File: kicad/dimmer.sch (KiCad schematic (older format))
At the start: 13 parts, among them J3 Load Out, J4 LED_BYPASS, U2 MOC3021M, U3 4N25

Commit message: Add some more descriptive text
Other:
- note added: "Dimming"
- note added: "Zero Crossing Detection"
- moved on the sheet: D1, D3, J3, J4, R10, R8, U2
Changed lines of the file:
@@
 Wire Wire Line
 	7100 3800 7350 3800
-Text Label 6750 2650 3    60   ~ 0
+Text Label 6750 2550 3    60   ~ 0
 ZeroCrossingOut
 $Comp
 L MOC3021M U2
 U 1 1 59BAEACD
-P 5900 4650
-F 0 "U2" H 5690 4840 50  0000 L CNN
-F 1 "MOC3021M" H 5900 4850 50  0000 L CNN
-F 2 "Housings_DIP:DIP-6_W7.62mm_LongPads" H 5700 4450 50  0001 L CIN
-F 3 "" H 5875 4650 50  0001 L CNN
-	1    5900 4650
+P 5900 5150
+F 0 "U2" H 5690 5340 50  0000 L CNN
+F 1 "MOC3021M" H 5900 5350 50  0000 L CNN
+F 2 "Housings_DIP:DIP-6_W7.62mm_LongPads" H 5700 4950 50  0001 L CIN
+F 3 "" H 5875 5150 50  0001 L CNN
+	1    5900 5150
 	-1   0    0    -1
 $EndComp
@@
 L Q_TRIAC_AAG D1
 U 1 1 59BAECA2
-P 4200 4700
-F 0 "D1" H 4325 4725 50  0000 L CNN
-F 1 "BT136X-600" H 4325 4650 50  0000 L CNN
-F 2 "TO_SOT_Packages_THT:TO-220_Vertical" V 4275 4725 50  0001 C CNN
-F 3 "" V 4200 4700 50  0001 C CNN
-	1    4200 4700
-	1    0    0    -1
-$EndComp
-Wire Wire Line
-	3850 2600 3850 4550
-Wire Wire Line
-	3850 4550 4900 4550
+P 4200 5200
+F 0 "D1" H 4325 5225 50  0000 L CNN
+F 1 "BT136X-600" H 4325 5150 50  0000 L CNN
+F 2 "TO_SOT_Packages_THT:TO-220_Vertical" V 4275 5225 50  0001 C CNN
+F 3 "" V 4200 5200 50  0001 C CNN
+	1    4200 5200
+	1    0    0    -1
+$EndComp
+Wire Wire Line
+	3850 2600 3850 5050
+Wire Wire Line
+	3850 5050 4900 5050
 Connection ~ 3850 3600
 Wire Wire Line
-	4200 4850 4200 5150
-Text Label 4450 5150 0    60   ~ 0
+	4200 5350 4200 5650
+Text Label 4450 5650 0    60   ~ 0
 DimmedLiveOut
 Wire Wire Line
-	4200 5150 5400 5150
+	4200 5650 5400 5650
 $Comp
 L R R8
 U 1 1 59BAFEEA
-P 5050 4550
-F 0 "R8" V 5130 4550 50  0000 C CNN
-F 1 "1k" V 5050 4550 50  0000 C CNN
-F 2 "Resistors_THT:R_Axial_DIN0207_L6.3mm_D2.5mm_P7.62mm_Horizontal" V 4980 4550 50  0001 C CNN
-F 3 "" H 5050 4550 50  0001 C CNN
-	1    5050 4550
+P 5050 5050
+F 0 "R8" V 5130 5050 50  0000 C CNN
+F 1 "1k" V 5050 5050 50  0000 C CNN
+F 2 "Resistors_THT:R_Axial_DIN0207_L6.3mm_D2.5mm_P7.62mm_Horizontal" V 4980 5050 50  0001 C CNN
+F 3 "" H 5050 5050 50  0001 C CNN
+	1    5050 5050
 	0    1    1    0
 $EndComp
-Connection ~ 4200 4550
-Wire Wire Line
-	5200 4550 5600 4550
-Wire Wire Line
-	5600 4750 5600 4950
-Wire Wire Line
-	5600 4950 3950 4950
-Wire Wire Line
-	3950 4950 3950 4800
-Wire Wire Line
-	3950 4800 4050 4800
+Connection ~ 4200 5050
+Wire Wire Line
+	5200 5050 5600 5050
+Wire Wire Line
+	5600 5250 5600 5450
+Wire Wire Line
+	5600 5450 3950 5450
+Wire Wire Line
+	3950 5450 3950 5300
+Wire Wire Line
+	3950 5300 4050 5300
 $Comp
 L Conn_01x03 J3
 U 1 1 59BB0206
-P 5600 5250
-F 0 "J3" H 5600 5450 50  0000 C CNN
-F 1 "Load Out" H 5600 5050 50  0000 C CNN
-F 2 "kiall:RS_Pro_10mm_Pitch_3_Way_PCB_Terminal_Block" H 5600 5250 50  0001 C CNN
-F 3 "" H 5600 5250 50  0001 C CNN
-	1    5600 5250
-	1    0    0    -1
-$EndComp
-Wire Wire Line
-	3750 2400 3750 5350
-Wire Wire Line
-	3750 5350 5400 5350
+P 5600 5750
+F 0 "J3" H 5600 5950 50  0000 C CNN
+F 1 "Load Out" H 5600 5550 50  0000 C CNN
+F 2 "kiall:RS_Pro_10mm_Pitch_3_Way_PCB_Terminal_Block" H 5600 5750 50  0001 C CNN
+F 3 "" H 5600 5750 50  0001 C CNN
+	1    5600 5750
+	1    0    0    -1
+$EndComp
+Wire Wire Line
+	3750 2400 3750 5850
+Wire Wire Line
+	3750 5850 5400 5850
 Connection ~ 3750 4000
 $Comp
 L LED D3
 U 1 1 59BB07F2
-P 6600 4550
-F 0 "D3" H 6600 4650 50  0000 C CNN
-F 1 "LED" H 6600 4450 50  0000 C CNN
-F 2 "LEDs:LED_D4.0mm" H 6600 4550 50  0001 C CNN
-F 3 "" H 6600 4550 50  0001 C CNN
-	1    6600 4550
-	1    0    0    -1
-$EndComp
-Wire Wire Line
-	6200 4550 6450 4550
+P 6600 5050
+F 0 "D3" H 6600 5150 50  0000 C CNN
+F 1 "LED" H 6600 4950 50  0000 C CNN
+F 2 "LEDs:LED_D4.0mm" H 6600 5050 50  0001 C CNN
+F 3 "" H 6600 5050 50  0001 C CNN
+	1    6600 5050
+	1    0    0    -1
+$EndComp
+Wire Wire Line
+	6200 5050 6450 5050
 $Comp
 L R R10
 U 1 1 59BB08C6
-P 7050 4550
-F 0 "R10" V 7130 4550 50  0000 C CNN
-F 1 "220" V 7050 4550 50  0000 C CNN
-F 2 "Resistors_SMD:R_1206_HandSoldering" V 6980 4550 50  0001 C CNN
-F 3 "" H 7050 4550 50  0001 C CNN
-	1    7050 4550
+P 7050 5050
+F 0 "R10" V 7130 5050 50  0000 C CNN
+F 1 "220" V 7050 5050 50  0000 C CNN
+F 2 "Resistors_SMD:R_1206_HandSoldering" V 6980 5050 50  0001 C CNN
+F 3 "" H 7050 5050 50  0001 C CNN
+	1    7050 5050
 	0    1    1    0
 $EndComp
 Wire Wire Line
-	6750 4550 6900 4550
-Text Label 7700 3300 1    60   ~ 0
+	6750 5050 6900 5050
+Text Label 7700 2550 3    60   ~ 0
 DimmerIn
 $Sheet
@@
 L GND #PWR03
 U 1 1 59BB3317
-P 6350 4750
-F 0 "#PWR03" H 6350 4500 50  0001 C CNN
-F 1 "GND" H 6350 4600 50  0000 C CNN
-F 2 "" H 6350 4750 50  0001 C CNN
-F 3 "" H 6350 4750 50  0001 C CNN
-	1    6350 4750
-	1    0    0    -1
-$EndComp
-Wire Wire Line
-	6350 4750 6200 4750
+P 6350 5250
+F 0 "#PWR03" H 6350 5000 50  0001 C CNN
+F 1 "GND" H 6350 5100 50  0000 C CNN
+F 2 "" H 6350 5250 50  0001 C CNN
+F 3 "" H 6350 5250 50  0001 C CNN
+	1    6350 5250
+	1    0    0    -1
+$EndComp
+Wire Wire Line
+	6350 5250 6200 5250
 Wire Wire Line
 	6750 2500 6750 3800
@@
 	6200 2250 7700 2250
 Wire Wire Line
-	7700 2250 7700 4550
-Wire Wire Line
-	7700 4550 7200 4550
+	7700 2250 7700 5050
+Wire Wire Line
+	7700 5050 7200 5050
 Wire Wire Line
 	5000 2600 4550 2600
@@
 L GS2 J4
 U 1 1 59BD7F23
-P 6600 4350
-F 0 "J4" H 6700 4500 50  0000 C CNN
-F 1 "LED_BYPASS" V 6700 4201 50  0000 C CNN
-F 2 "Connectors:GS2" V 6674 4350 50  0001 C CNN
-F 3 "" H 6600 4350 50  0001 C CNN
-	1    6600 4350
+P 6600 4850
+F 0 "J4" H 6700 5000 50  0000 C CNN
+F 1 "LED_BYPASS" V 6700 4701 50  0000 C CNN
+F 2 "Connectors:GS2" V 6674 4850 50  0001 C CNN
+F 3 "" H 6600 4850 50  0001 C CNN
+	1    6600 4850
 	0    -1   -1   0
 $EndComp
 Wire Wire Line
-	6800 4350 6800 4550
-Connection ~ 6800 4550
-Wire Wire Line
-	6400 4350 6400 4550
-Connection ~ 6400 4550
+	6800 4850 6800 5050
+Connection ~ 6800 5050
+Wire Wire Line
+	6400 4850 6400 5050
+Connection ~ 6400 5050
 Wire Wire Line
 	5000 2200 3650 2200
 Wire Wire Line
-	3650 2200 3650 5250
-Wire Wire Line
-	3650 5250 5400 5250
+	3650 2200 3650 5750
+Wire Wire Line
+	3650 5750 5400 5750
+Wire Notes Line
+	3500 3350 7850 3350
+Wire Notes Line
+	3500 3350 3500 4350
+Wire Notes Line
+	3500 4350 7850 4350
+Wire Notes Line
+	7850 4350 7850 3350
+Wire Notes Line
+	7850 4650 3500 4650
+Wire Notes Line
+	3500 4650 3500 6100
+Wire Notes Line
+	3500 6100 7850 6100
+Wire Notes Line
+	7850 6100 7850 4650
+Text Notes 4000 3350 0    60   ~ 0
+Zero Crossing Detection
+Text Notes 4000 4650 0    60   ~ 0
+Dimming
 $EndSCHEMATC

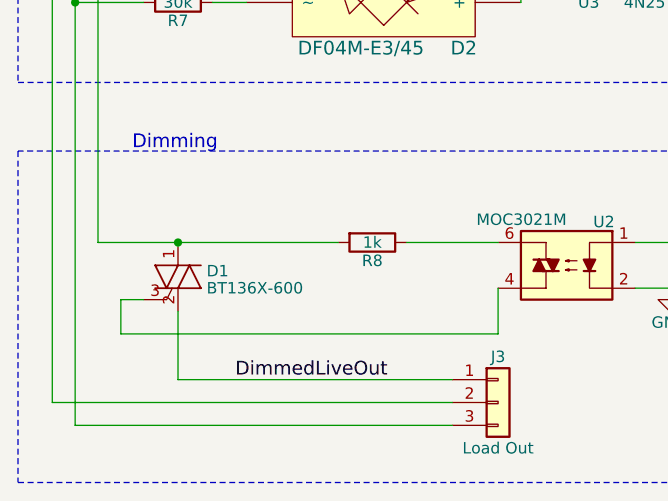
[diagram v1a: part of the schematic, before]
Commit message: Rev 1.1: Fix triac connections
Pins 1 and 2 on the triac D1 were connected in backwords, preventing
the circuit from working.
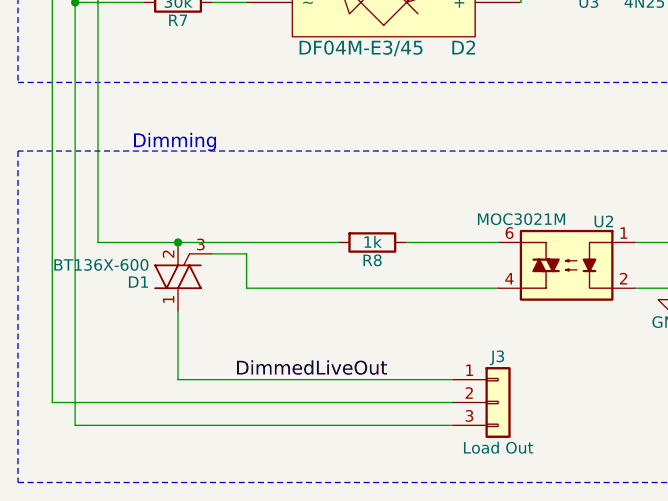
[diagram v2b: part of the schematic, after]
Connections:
- net DimmedLiveOut: now also D1.1 (A1); no longer D1.2 (A2)
- net at F1.2, R6.2, R8.2: now also D1.2 (A2); no longer D1.1 (A1)
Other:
- moved on the sheet: D1
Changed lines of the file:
@@
 Title "ESP8266 ESP-03 Lighting Dimmer"
 Date ""
-Rev "1.0"
+Rev "1.1"
 Comp "Kiall Mac Inness"
 Comment1 ""
@@
 F 3 "" V 4200 5200 50  0001 C CNN
 	1    4200 5200
-	1    0    0    -1
+	-1   0    0    1
 $EndComp
 Wire Wire Line
@@
 Wire Wire Line
 	5200 5050 5600 5050
-Wire Wire Line
-	5600 5250 5600 5450
-Wire Wire Line
-	5600 5450 3950 5450
-Wire Wire Line
-	3950 5450 3950 5300
-Wire Wire Line
-	3950 5300 4050 5300
 $Comp
 L Conn_01x03 J3
@@
 Text Notes 4000 4650 0    60   ~ 0
 Dimming
+Wire Wire Line
+	5600 5250 4500 5250
+Wire Wire Line
+	4500 5250 4500 5100
+Wire Wire Line
+	4500 5100 4350 5100
 $EndSCHEMATC

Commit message: Update for v1.2 - Fixes and board redesign
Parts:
- removed D3: LED, LEDs:LED_D4.0mm, symbol LED
- removed J4: LED_BYPASS, Connectors:GS2, symbol GS2
- D1: footprint TO_SOT_Packages_THT:TO-220_Vertical -> TO_SOT_Packages_THT:TO-220-3_Vertical
- U3: footprint Housings_DIP:DIP-6_W7.62mm_SMD -> Housings_DIP:SMDIP-6_W9.53mm
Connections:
- net at U2.1: now also R10.2
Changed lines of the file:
@@
 Title "ESP8266 ESP-03 Lighting Dimmer"
 Date ""
-Rev "1.1"
+Rev "1.2"
 Comp "Kiall Mac Inness"
 Comment1 ""
@@
 F 0 "U3" H 5950 4000 50  0000 L CNN
 F 1 "4N25" H 6150 4000 50  0000 L CNN
-F 2 "Housings_DIP:DIP-6_W7.62mm_SMD" H 5950 3600 50  0001 L CIN
+F 2 "Housings_DIP:SMDIP-6_W9.53mm" H 5950 3600 50  0001 L CIN
 F 3 "" H 6150 3800 50  0001 L CNN
 	1    6150 3800
@@
 F 0 "D1" H 4325 5225 50  0000 L CNN
 F 1 "BT136X-600" H 4325 5150 50  0000 L CNN
-F 2 "TO_SOT_Packages_THT:TO-220_Vertical" V 4275 5225 50  0001 C CNN
+F 2 "TO_SOT_Packages_THT:TO-220-3_Vertical" V 4275 5225 50  0001 C CNN
 F 3 "" V 4200 5200 50  0001 C CNN
 	1    4200 5200
@@
 	3750 5850 5400 5850
 Connection ~ 3750 4000
-$Comp
-L LED D3
-U 1 1 59BB07F2
-P 6600 5050
-F 0 "D3" H 6600 5150 50  0000 C CNN
-F 1 "LED" H 6600 4950 50  0000 C CNN
-F 2 "LEDs:LED_D4.0mm" H 6600 5050 50  0001 C CNN
-F 3 "" H 6600 5050 50  0001 C CNN
-	1    6600 5050
-	1    0    0    -1
-$EndComp
-Wire Wire Line
-	6200 5050 6450 5050
+Wire Wire Line
+	6200 5050 6900 5050
 $Comp
 L R R10
@@
 	0    1    1    0
 $EndComp
-Wire Wire Line
-	6750 5050 6900 5050
 Text Label 7700 2550 3    60   ~ 0
 DimmerIn
@@
 Wire Wire Line
 	3750 4000 4050 4000
-$Comp
-L GS2 J4
-U 1 1 59BD7F23
-P 6600 4850
-F 0 "J4" H 6700 5000 50  0000 C CNN
-F 1 "LED_BYPASS" V 6700 4701 50  0000 C CNN
-F 2 "Connectors:GS2" V 6674 4850 50  0001 C CNN
-F 3 "" H 6600 4850 50  0001 C CNN
-	1    6600 4850
-	0    -1   -1   0
-$EndComp
-Wire Wire Line
-	6800 4850 6800 5050
-Connection ~ 6800 5050
-Wire Wire Line
-	6400 4850 6400 5050
-Connection ~ 6400 5050
 Wire Wire Line
 	5000 2200 3650 2200
